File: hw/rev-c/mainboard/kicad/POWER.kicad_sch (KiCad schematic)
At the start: 75 parts, among them J10 5V PWR, J11 9V POWER, J12 9V POWER, J8 PET POWER, U23 TPS5430DDA, U3 AMS1117-3.3, U4 XL1509-5.0E1, U5 LM317AG-TN3-R, U6 LM317AG-TN3-R

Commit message: hw: TPS5430 buck converter
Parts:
- removed C103, C13, C2: 22u, Capacitor_SMD:C_0805_2012Metric, symbol Device:C_Small
- removed C105: 100n, Capacitor_SMD:C_0402_1005Metric, symbol Device:C_Small
- removed C109: 47n, Capacitor_SMD:C_0603_1608Metric, symbol Device:C_Small
- removed C113: 470p, Capacitor_SMD:C_0603_1608Metric, symbol Device:C_Small
- removed C15: 1u, Capacitor_SMD:C_0402_1005Metric, symbol Device:C_Small
- removed C3, C5, C6: 47u 10V, Capacitor_SMD:C_1206_3216Metric, symbol Device:C_Small
- removed D5: SS54, Diode_SMD:D_SMA, symbol Device:D_Schottky_Small
- removed L1: 68uH, JLCPCB:IND-SMD_L11.5-W10.0_SMMS1040, symbol Device:L
- removed U4: XL1509-5.0E1, Package_SO:SOP-8_3.9x4.9mm_P1.27mm, symbol EconoPET:XL1509-5.0E1
- C110: value 47u 10V -> 10u; footprint Capacitor_SMD:C_1206_3216Metric -> Capacitor_SMD:C_0603_1608Metric; LCSC C96123 -> C96446
- C2: renamed from C106; value 100p -> 150p; LCSC C1546 -> C1527
- C3: renamed from C108; value 100n -> 220n; LCSC C1525 -> C16772
- C4: value 47u 10V -> 22u; footprint Capacitor_SMD:C_1206_3216Metric -> Capacitor_SMD:C_0805_2012Metric; LCSC C96123 -> C45783
- C5: renamed from C112; value 1n -> 2.2n; LCSC C1523 -> C1531
- L1: renamed from L2; value 15uH -> 22uH; footprint JLCPCB:IND-SMD_L11.5-W10.5_MWSA1004 -> JLCPCB:IND-SMD_L12.5-W12.5; LCSC C151872 -> C2924827
- R61: value 470 -> 220; LCSC C25117 -> C25091
- renumbered D13 to D5, U23 to U4
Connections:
- net +5V: no longer C1.1, C4.1
- net +9V_Unreg: now also C1.1, C4.1
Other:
- note removed: "I_{LOAD} = 2A DUTY = ~5V/9V = ~0.56 I_{IN} = I_{LOAD} * (1 - DUTY) = ~0.9A I_{OUT} = I_{LOAD} * DUTY = ~1.1A"
- moved on the sheet: C1, C107, C11, C110, C111, C12, C2, C3, C5, D5, L1, R61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

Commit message: hw: reduce +6V thermal vias
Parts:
- U4: footprint Package_SO:TI_SO-PowerPAD-8_ThermalVias -> EconoPET:TI_SO-PowerPAD-8_ThermalVias
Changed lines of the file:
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@@
 			)
 		)
-		(property "Footprint" "Package_SO:TI_SO-PowerPAD-8_ThermalVias"
+		(property "Footprint" "EconoPET:TI_SO-PowerPAD-8_ThermalVias"
 			(at 176.53 93.98 0)
 			(effects

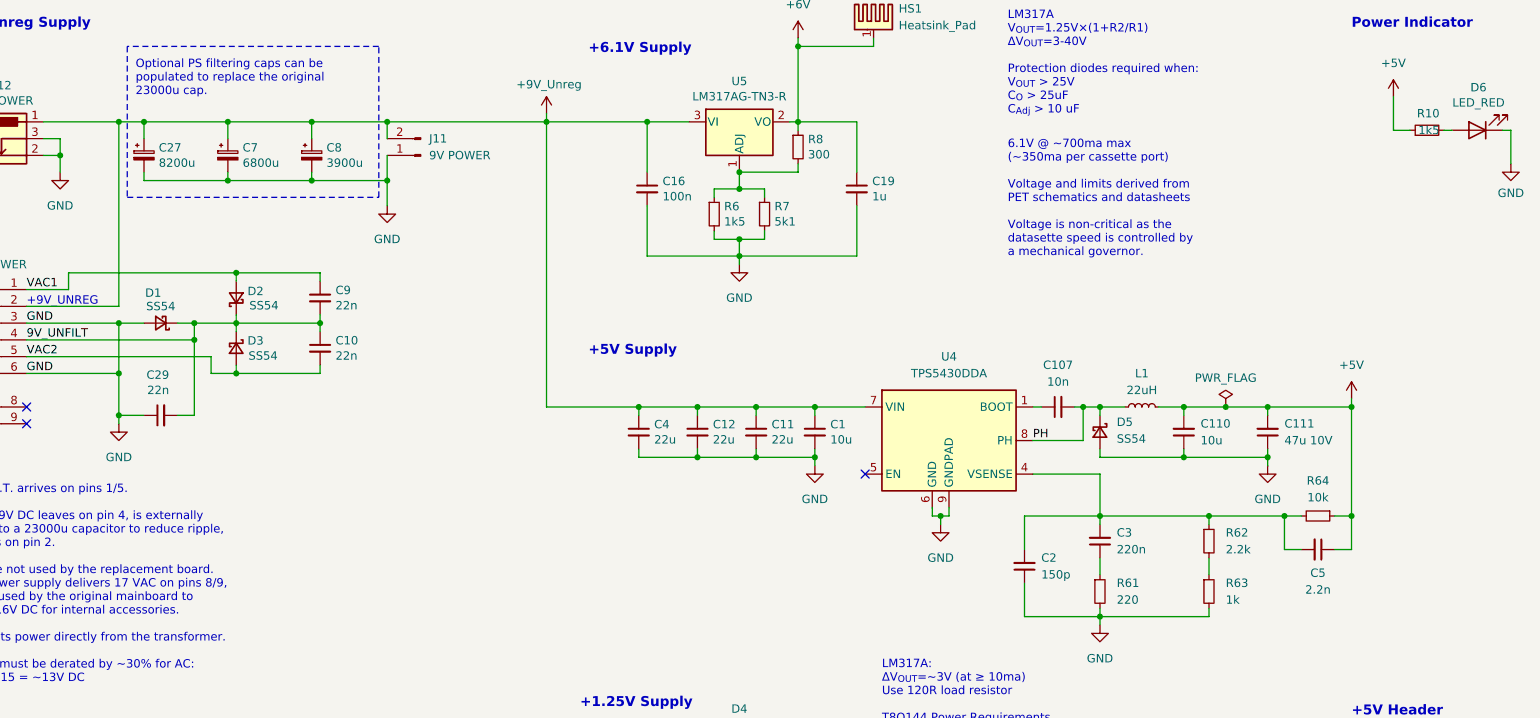
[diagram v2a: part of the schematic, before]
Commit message: hw: rework buck converter (wip)
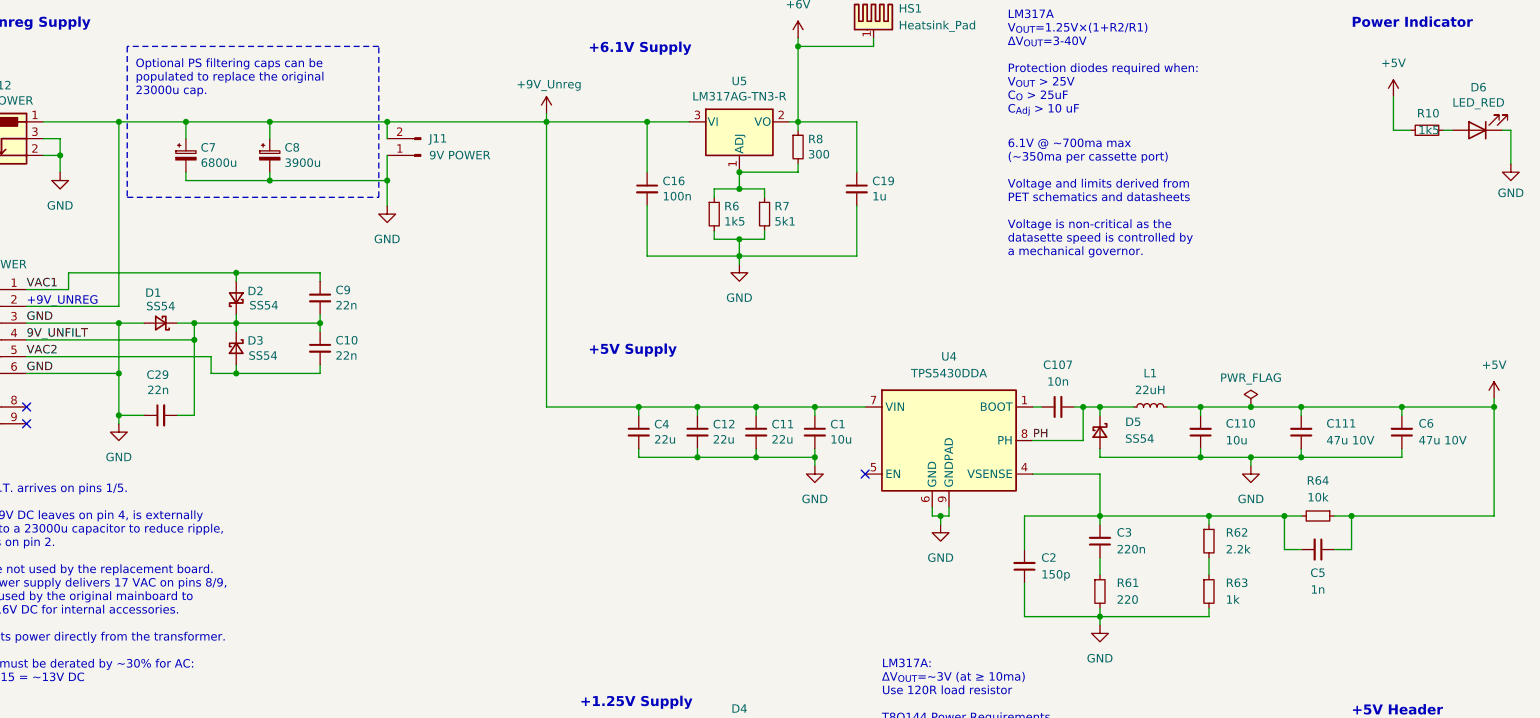
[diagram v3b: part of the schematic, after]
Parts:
- removed C27: 8200u, PET:CP_Radial_D18.0mm_P5.00mm_P7.50mm, symbol Device:C_Polarized_Small
- added C6: 47u 10V, Capacitor_SMD:C_1206_3216Metric, symbol Device:C_Small
- C5: value 2.2n -> 1n; LCSC C1531 -> C1523
- C7: footprint PET:CP_Radial_D16.0mm_P5.00mm_P7.50mm -> EconoPET:CP_Radial_D24.0mm_P5.00mm_P7.50mm_P10.00mm_SnapIn
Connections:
- net +5V: now also C6.2
- net GND: now also C6.1
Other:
- moved on the sheet: C110, C111, C7, C8, L1

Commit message: hw: renumber reference designators
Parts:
- renumbered C14 to C10, C5 to C11, C3 to C12, C2 to C13, C18 to C15, C29 to C17, C19 to C18, C21 to C19, C11 to C2, C7 to C20, C8 to C21, C25 to C22, C9 to C23, C26 to C24, C16 to C25, C28 to C26, C17 to C27, C12 to C3, C107 to C5, C110 to C6, C111 to C7, C6 to C8, C10 to C9, D5 to D2, D2 to D5, J12 to J1, J8 to J2, J11 to J3, J10 to J4, R9 to R10, R5 to R12, R6 to R13, R7 to R14, R10 to R15, R64 to R4, R63 to R5, R62 to R6, R61 to R7, R60 to R8, R8 to R9, U5 to U4, U6 to U5, U4 to U6

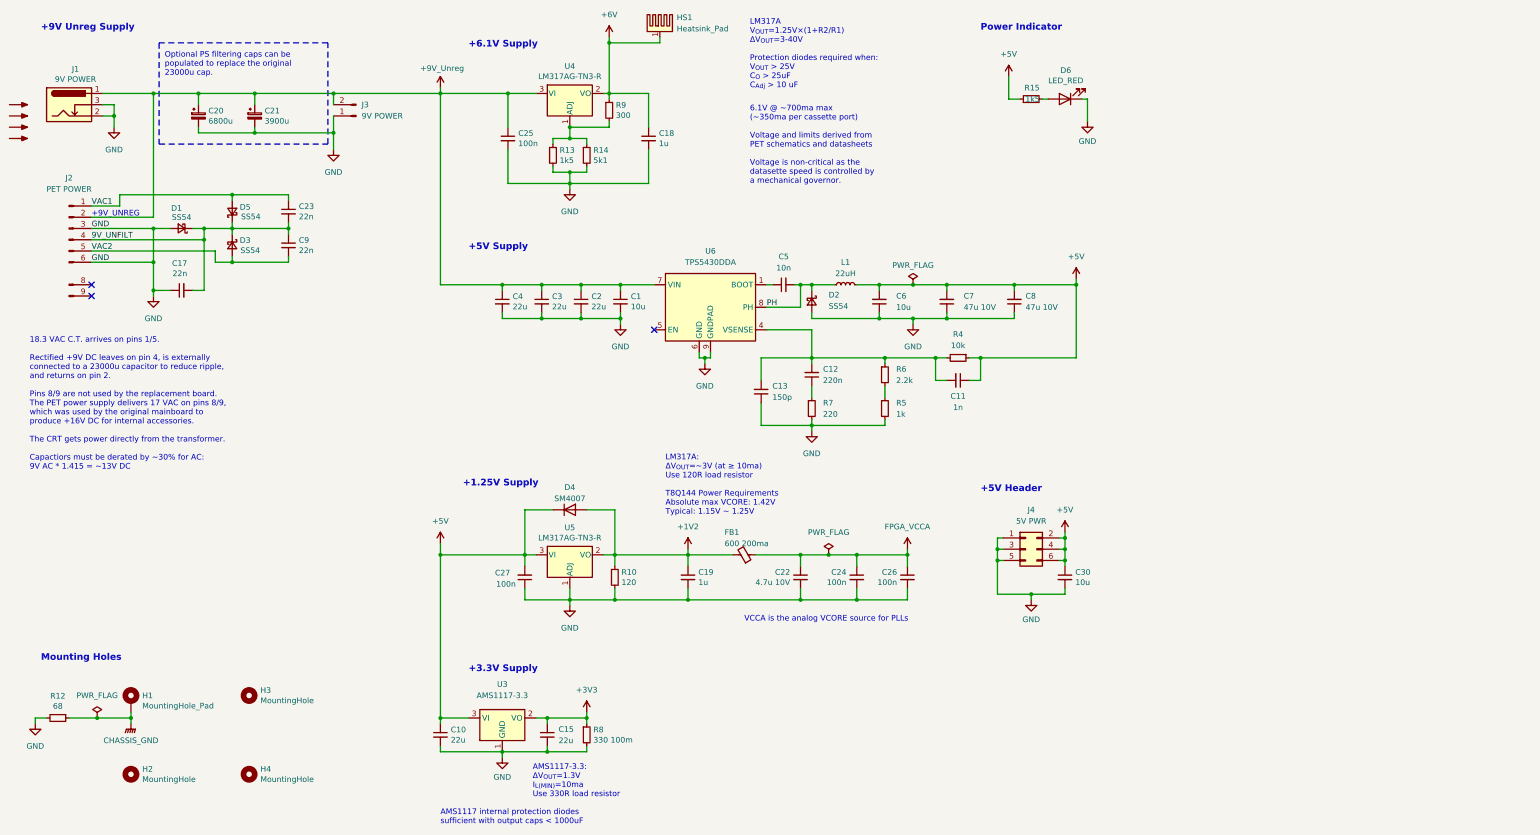
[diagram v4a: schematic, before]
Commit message: hw: header for 5v/video select, ESR for AMS1117 + tidy
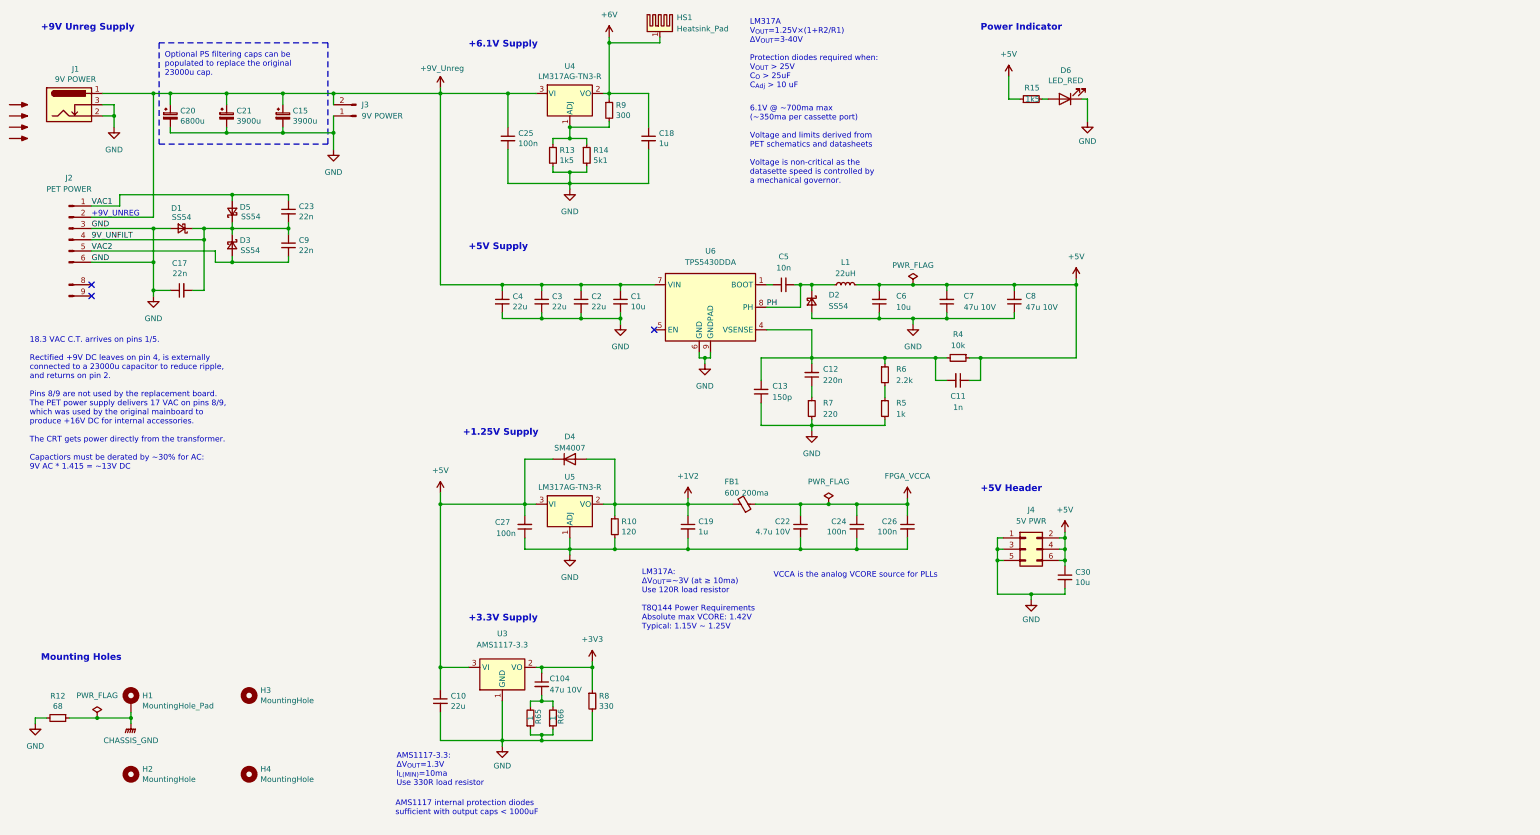
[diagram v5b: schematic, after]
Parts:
- removed C15: 22u, Capacitor_SMD:C_0805_2012Metric, symbol Device:C_Small
- added C104: 47u 10V, Capacitor_SMD:C_1206_3216Metric, symbol Device:C_Small
- added C15: 3900u, EconoPET:CP_Radial_D8.0mm_P3.50mm_P5.00mm, symbol Device:C_Polarized_Small
- added R65, R66: 1, Resistor_SMD:R_0603_1608Metric, symbol Device:R_Small
- R8: value 330 100m -> 330
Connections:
- net +3V3: now also C104.1
- net +9V_Unreg: now also C15.1
- net GND: now also C15.2, R65.1, R66.1
- new net: C104.2, R65.2, R66.2
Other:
- moved on the sheet: C10, C19, C20, C21, C22, C24, C26, C27, D4, FB1, R10, R8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

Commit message: hw: match original PET designators for connectors
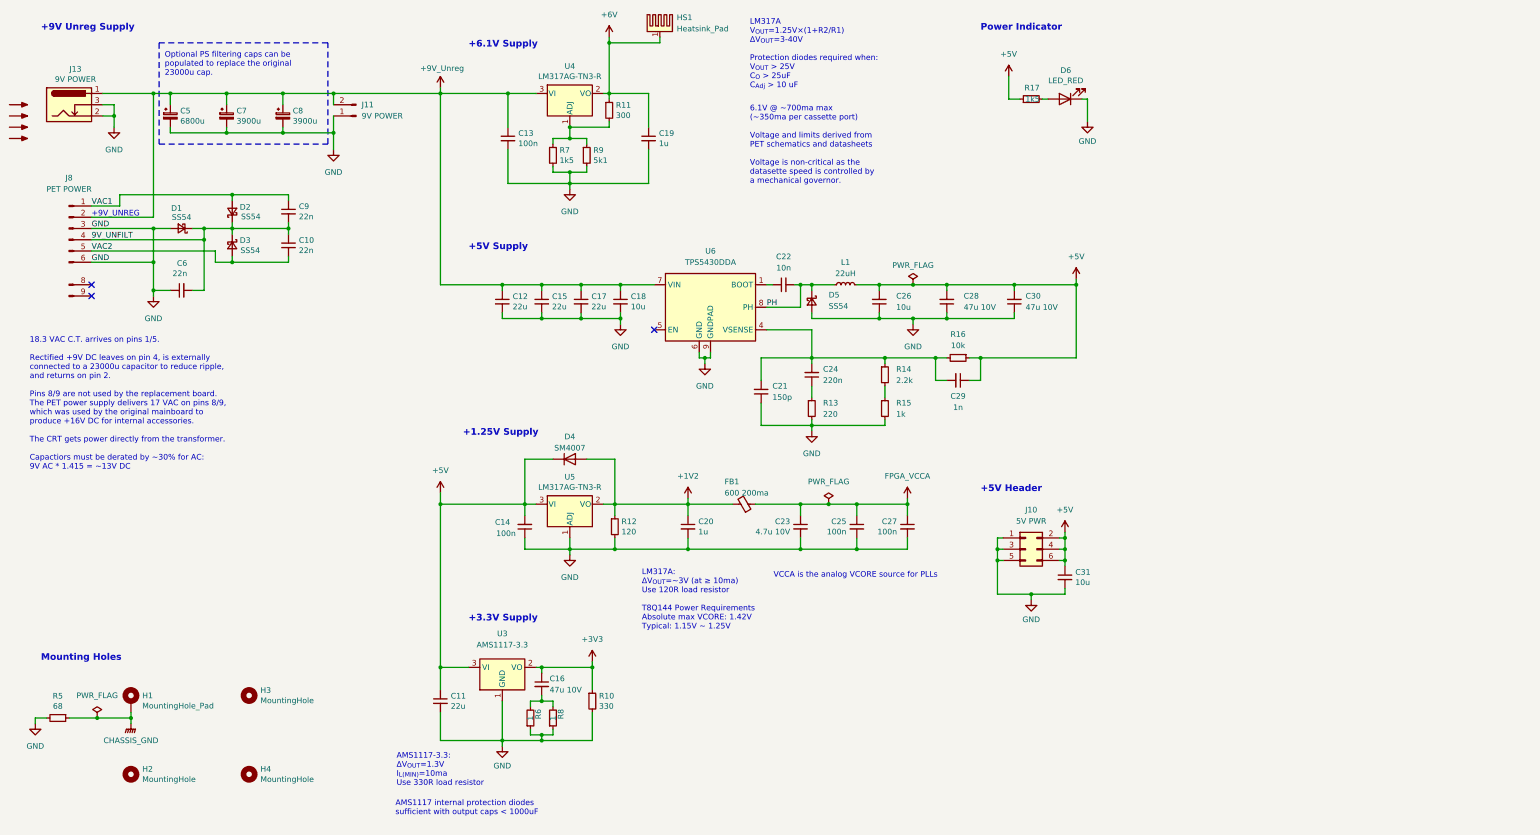
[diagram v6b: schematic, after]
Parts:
- renumbered C9 to C10, C10 to C11, C4 to C12, C25 to C13, C27 to C14, C3 to C15, C104 to C16, C2 to C17, C1 to C18, C18 to C19, C19 to C20, C13 to C21, C5 to C22, C22 to C23, C12 to C24, C24 to C25, C6 to C26, C26 to C27, C7 to C28, C11 to C29, C8 to C30, C30 to C31, C20 to C5, C17 to C6, C21 to C7, C15 to C8, C23 to C9, D5 to D2, D2 to D5, J4 to J10, J3 to J11, J1 to J13, J2 to J8, R8 to R10, R9 to R11, R10 to R12, R7 to R13, R6 to R14, R5 to R15, R4 to R16, R15 to R17, R12 to R5, R65 to R6, R13 to R7, R66 to R8, R14 to R9

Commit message: hw: perimeter stitching (wip)
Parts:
- removed C8: 3900u, EconoPET:CP_Radial_D8.0mm_P3.50mm_P5.00mm, symbol Device:C_Polarized_Small
- C5: value 6800u -> 15000u; MOUSER 661-EKYB250E682ML40S -> 661-BV250L153AM40S
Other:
- moved on the sheet: C5, C7
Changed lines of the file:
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@@
 	)
 	(junction
-		(at 53.34 36.83)
+		(at 59.69 36.83)
 		(diameter 0)
 		(color 0 0 0 0)
@@
 	)
 	(junction
-		(at 66.04 45.72)
+		(at 72.39 45.72)
 		(diameter 0)
 		(color 0 0 0 0)
@@
 	)
 	(junction
-		(at 78.74 45.72)
-		(diameter 0)
-		(color 0 0 0 0)
-	)
-	(junction
 		(at 255.27 142.24)
 		(diameter 0)
@@
 	)
 	(junction
-		(at 78.74 36.83)
-		(diameter 0)
-		(color 0 0 0 0)
-	)
-	(junction
 		(at 137.16 181.61)
 		(diameter 0)
@@
 	)
 	(junction
-		(at 66.04 36.83)
+		(at 72.39 36.83)
 		(diameter 0)
 		(color 0 0 0 0)
@@
 	(wire
 		(pts
-			(xy 53.34 36.83) (xy 66.04 36.83)
+			(xy 59.69 36.83) (xy 72.39 36.83)
 		)
 		(stroke
@@
 	(wire
 		(pts
-			(xy 66.04 44.45) (xy 66.04 45.72)
+			(xy 72.39 44.45) (xy 72.39 45.72)
 		)
 		(stroke
@@
 	(wire
 		(pts
-			(xy 78.74 45.72) (xy 90.17 45.72)
+			(xy 72.39 45.72) (xy 90.17 45.72)
 		)
 		(stroke
@@
 	(wire
 		(pts
-			(xy 66.04 36.83) (xy 66.04 39.37)
+			(xy 72.39 36.83) (xy 72.39 39.37)
 		)
 		(stroke
@@
 	(wire
 		(pts
-			(xy 78.74 36.83) (xy 90.17 36.83)
-		)
-		(stroke
-			(width 0)
-			(type default)
-		)
-	)
-	(wire
-		(pts
 			(xy 213.36 87.63) (xy 220.98 87.63)
 		)
@@
 	(wire
 		(pts
-			(xy 78.74 44.45) (xy 78.74 45.72)
-		)
-		(stroke
-			(width 0)
-			(type default)
-		)
-	)
-	(wire
-		(pts
 			(xy 41.91 59.69) (xy 41.91 62.23)
 		)
@@
 	(wire
 		(pts
-			(xy 53.34 45.72) (xy 53.34 44.45)
+			(xy 59.69 45.72) (xy 59.69 44.45)
 		)
 		(stroke
@@
 	(wire
 		(pts
-			(xy 49.53 36.83) (xy 53.34 36.83)
+			(xy 49.53 36.83) (xy 59.69 36.83)
 		)
 		(stroke
@@
 	(wire
 		(pts
-			(xy 53.34 36.83) (xy 53.34 39.37)
+			(xy 59.69 36.83) (xy 59.69 39.37)
 		)
 		(stroke
@@
 	(wire
 		(pts
-			(xy 53.34 45.72) (xy 66.04 45.72)
+			(xy 59.69 45.72) (xy 72.39 45.72)
 		)
 		(stroke
@@
 	(wire
 		(pts
-			(xy 66.04 36.83) (xy 78.74 36.83)
-		)
-		(stroke
-			(width 0)
-			(type default)
-		)
-	)
-	(wire
-		(pts
-			(xy 78.74 36.83) (xy 78.74 39.37)
+			(xy 72.39 36.83) (xy 90.17 36.83)
 		)
 		(stroke
@@
 	(wire
 		(pts
-			(xy 66.04 45.72) (xy 78.74 45.72)
-		)
-		(stroke
-			(width 0)
-			(type default)
-		)
-	)
-	(wire
-		(pts
 			(xy 133.35 139.7) (xy 143.51 139.7)
 		)
@@
 	(symbol
 		(lib_id "Device:C_Polarized_Small")
-		(at 66.04 41.91 0)
+		(at 72.39 41.91 0)
 		(unit 1)
 		(exclude_from_sim no)
@@
 		(dnp no)
 		(property "Reference" "C7"
-			(at 68.2752 40.7416 0)
+			(at 74.6252 40.7416 0)
 			(effects
 				(font
@@
 		)
 		(property "Value" "3900u"
-			(at 68.2752 43.053 0)
+			(at 74.6252 43.053 0)
 			(effects
 				(font
@@
 		)
 		(property "Footprint" "Capacitor_THT:CP_Radial_D12.5mm_P5.00mm"
-			(at 66.04 41.91 0)
+			(at 72.39 41.91 0)
 			(effects
 				(font
@@
 		)
 		(property "Datasheet" "https://www.mouser.com/datasheet/2/420/Chemi_Con_KYBLL_e-3313623.pdf"
-			(at 66.04 41.91 0)
+			(at 72.39 41.91 0)
 			(effects
 				(font
@@
 		)
 		(property "Description" ""
-			(at 66.04 41.91 0)
+			(at 72.39 41.91 0)
 			(effects
 				(font
@@
 		)
 		(property "MOUSER" "661-EKYB250E392MK40S"
-			(at 66.04 41.91 0)
+			(at 72.39 41.91 0)
 			(effects
 				(font
@@
 			)
 		)
-		(property "Datasheet" "https://datasheet.lcsc.com/lcsc/2304140030_Samsung-Electro-Mechanics-CL05A475MP5NRNC_C23733.pdf"
+		(property "Datasheet" "https://product.samsungsem.com/mlcc/CL05A475MP5NRN.do"
 			(at 195.58 134.62 0)
 			(effects
@@
 	(symbol
 		(lib_id "Device:C_Polarized_Small")
-		(at 53.34 41.91 0)
+		(at 59.69 41.91 0)
 		(unit 1)
 		(exclude_from_sim no)
@@
 		(dnp no)
 		(property "Reference" "C5"
-			(at 55.5752 40.7416 0)
+			(at 61.9252 40.7416 0)
 			(effects
 				(font
@@
 			)
 		)
-		(property "Value" "6800u"
-			(at 55.5752 43.053 0)
+		(property "Value" "15000u"
+			(at 61.9252 43.053 0)
 			(effects
 				(font
@@
 		)
 		(property "Footprint" "EconoPET:CP_Radial_D24.0mm_P5.00mm_P7.50mm_P10.00mm_SnapIn"
-			(at 53.34 41.91 0)
+			(at 59.69 41.91 0)
 			(effects
 				(font
@@
 			)
 		)
-		(property "Datasheet" "https://www.mouser.com/datasheet/2/420/Chemi_Con_KYBLL_e-3313623.pdf"
-			(at 53.34 41.91 0)
+		(property "Datasheet" "https://www.chemi-con.co.jp/products/relatedfiles/capacitor/catalog/LBVLL-e.PDF"
+			(at 59.69 41.91 0)
 			(effects
 				(font
@@
 		)
 		(property "Description" ""
-			(at 53.34 41.91 0)
+			(at 59.69 41.91 0)
 			(effects
 				(font
@@
 			)
 		)
-		(property "MOUSER" "661-EKYB250E682ML40S"
-			(at 53.34 41.91 0)
+		(property "MOUSER" "661-BV250L153AM40S"
+			(at 59.69 41.91 0)
 			(effects
 				(font
@@
 					(unit 1)
 				)
-			)
-		)
-	)
-	(symbol
-		(lib_id "Device:C_Polarized_Small")
-		(at 78.74 41.91 0)
-		(unit 1)
-		(exclude_from_sim no)
-		(in_bom yes)
-		(on_board yes)
-		(dnp no)
-		(property "Reference" "C8"
-			(at 80.9752 40.7416 0)
-			(effects
-				(font
-					(size 1.27 1.27)
-				)
-				(justify left)
-			)
-		)
-		(property "Value" "3900u"
-			(at 80.9752 43.053 0)
-			(effects
-				(font
-					(size 1.27 1.27)
-				)
-				(justify left)
-			)
-		)
-		(property "Footprint" "EconoPET:CP_Radial_D8.0mm_P3.50mm_P5.00mm"
-			(at 78.74 41.91 0)
-			(effects
-				(font
-					(size 1.27 1.27)
-				)
-				(hide yes)
-			)
-		)
-		(property "Datasheet" "https://www.mouser.com/datasheet/2/420/Chemi_Con_KYBLL_e-3313623.pdf"
-			(at 78.74 41.91 0)
-			(effects
-				(font
-					(size 1.27 1.27)
-				)
-				(hide yes)
-			)
-		)
-		(property "Description" ""
-			(at 78.74 41.91 0)
-			(effects
-				(font
-					(size 1.27 1.27)
-				)
-				(hide yes)
-			)
-		)
-		(property "MOUSER" "661-EKYB250E392MK40S"
-			(at 78.74 41.91 0)
-			(effects
-				(font
-					(size 1.27 1.27)
-				)
-				(hide yes)
-			)
-		)
-		(pin "1"
-		)
-		(pin "2"
-		)
-		(instances
-			(project "Mainboard"
-				(path "/2eea20e6-112c-411a-b615-885ae773135a/00000000-0000-0000-0000-000061ed99de"
-					(reference "C8")
-					(unit 1)
-				)
